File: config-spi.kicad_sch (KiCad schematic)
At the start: 40 parts, among them J1 878321412, Q7 BSS138APW, Q8 BSS138APW, U15 XC7K160T-FFG676, U3 S25FL128SAGNFI000

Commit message: Update PCB naming
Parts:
- C12: footprint data-center-dram-tester-footprints:0603-cap -> data-center-rdimm-ddr4-tester-footprints:0603-cap; symbol data-center-dram-tester:C_47u_0603 -> data-center-rdimm-ddr4-tester:C_47u_0603
- C13, C37: footprint data-center-dram-tester-footprints:0402-cap -> data-center-rdimm-ddr4-tester-footprints:0402-cap; symbol data-center-dram-tester:C_470n_0402 -> data-center-rdimm-ddr4-tester:C_470n_0402
- C5: footprint data-center-dram-tester-footprints:0402-cap -> data-center-rdimm-ddr4-tester-footprints:0402-cap; symbol data-center-dram-tester:C_100n_0402 -> data-center-rdimm-ddr4-tester:C_100n_0402
- D1, D10: footprint data-center-dram-tester-footprints:LED_0603 -> data-center-rdimm-ddr4-tester-footprints:LED_0603; symbol data-center-dram-tester:KP-1608CGCK -> data-center-rdimm-ddr4-tester:KP-1608CGCK
- D4: footprint data-center-dram-tester-footprints:TPD6E05U06 -> data-center-rdimm-ddr4-tester-footprints:TPD6E05U06; symbol data-center-dram-tester:TPD6E05U06 -> data-center-rdimm-ddr4-tester:TPD6E05U06
- EMCCLK1, PUDC_B1: footprint data-center-dram-tester-footprints:Testpoint_smd_1mm -> data-center-rdimm-ddr4-tester-footprints:Testpoint_smd_1mm; symbol data-center-dram-tester:TP_SMD1MM -> data-center-rdimm-ddr4-tester:TP_SMD1MM
- J1: footprint data-center-dram-tester-footprints:PinHeader_2x7_P2mm_SMD_no_locator -> data-center-rdimm-ddr4-tester-footprints:PinHeader_2x7_P2mm_SMD_no_locator; symbol data-center-dram-tester:878321412 -> data-center-rdimm-ddr4-tester:878321412
- PROG_B1: footprint data-center-dram-tester-footprints:Switch_Tactile_SMD_B3U-1000P -> data-center-rdimm-ddr4-tester-footprints:Switch_Tactile_SMD_B3U-1000P; symbol data-center-dram-tester:B3U-1000P -> data-center-rdimm-ddr4-tester:B3U-1000P
- Q7, Q8: footprint data-center-dram-tester-footprints:SC70-3 -> data-center-rdimm-ddr4-tester-footprints:SC70-3; symbol data-center-dram-tester:BSS138APW -> data-center-rdimm-ddr4-tester:BSS138APW
- R10, R33, R34, R36: footprint data-center-dram-tester-footprints:0402-res -> data-center-rdimm-ddr4-tester-footprints:0402-res; symbol data-center-dram-tester:R_100R_0402 -> data-center-rdimm-ddr4-tester:R_100R_0402
- R11, R12, R13, R23, R24, R26, R27, R58, R59, R60, R9: footprint data-center-dram-tester-footprints:0402-res -> data-center-rdimm-ddr4-tester-footprints:0402-res; symbol data-center-dram-tester:R_0R_0402 -> data-center-rdimm-ddr4-tester:R_0R_0402
- R14: footprint data-center-dram-tester-footprints:0402-res -> data-center-rdimm-ddr4-tester-footprints:0402-res; symbol data-center-dram-tester:R_2k2_0402 -> data-center-rdimm-ddr4-tester:R_2k2_0402
- R193: footprint data-center-dram-tester-footprints:0402-res -> data-center-rdimm-ddr4-tester-footprints:0402-res; symbol data-center-dram-tester:R_10k_0402 -> data-center-rdimm-ddr4-tester:R_10k_0402
- R21, R22, R28, R32: footprint data-center-dram-tester-footprints:0402-res -> data-center-rdimm-ddr4-tester-footprints:0402-res; symbol data-center-dram-tester:R_4k7_0402 -> data-center-rdimm-ddr4-tester:R_4k7_0402
- R30, R31, R57: footprint data-center-dram-tester-footprints:0402-res -> data-center-rdimm-ddr4-tester-footprints:0402-res; symbol data-center-dram-tester:R_330R_0402 -> data-center-rdimm-ddr4-tester:R_330R_0402
- S2: footprint data-center-dram-tester-footprints:SW_DS04-254-1-01BK-SMT -> data-center-rdimm-ddr4-tester-footprints:SW_DS04-254-1-01BK-SMT; symbol data-center-dram-tester:DS04-254-1-01BK-SMT -> data-center-rdimm-ddr4-tester:DS04-254-1-01BK-SMT
- U15: footprint data-center-dram-tester-footprints:xc7k160tfbg676 -> data-center-rdimm-ddr4-tester-footprints:xc7k160tfbg676; symbol data-center-dram-tester:XC7K160T-FFG676 -> data-center-rdimm-ddr4-tester:XC7K160T-FFG676
- U3: footprint data-center-dram-tester-footprints:WSON8x6_WSON6x5_dual -> data-center-rdimm-ddr4-tester-footprints:WSON8x6_WSON6x5_dual; symbol data-center-dram-tester:S25FL128SAGNFI000 -> data-center-rdimm-ddr4-tester:S25FL128SAGNFI000
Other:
- title: Data Center DRAM Tester -> Data Center RDIMM DDR4 Tester

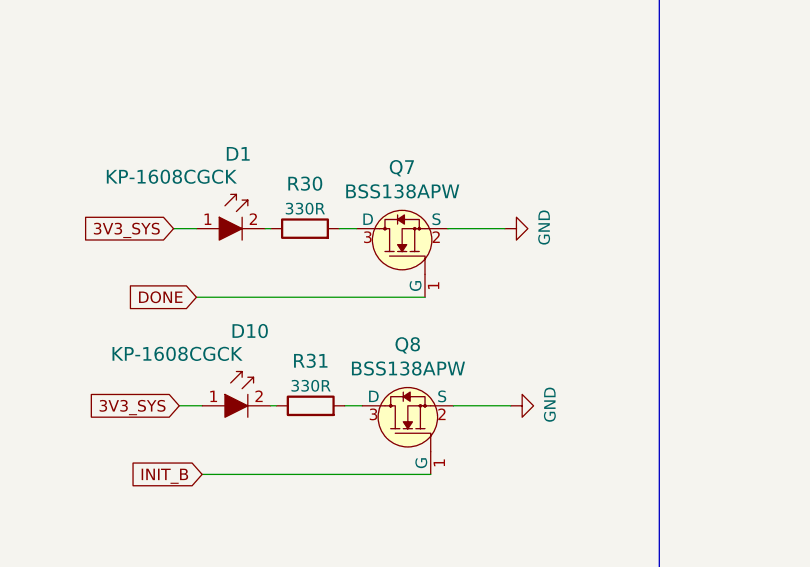
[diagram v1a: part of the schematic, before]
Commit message: Update BSS138PW lib name and MPN
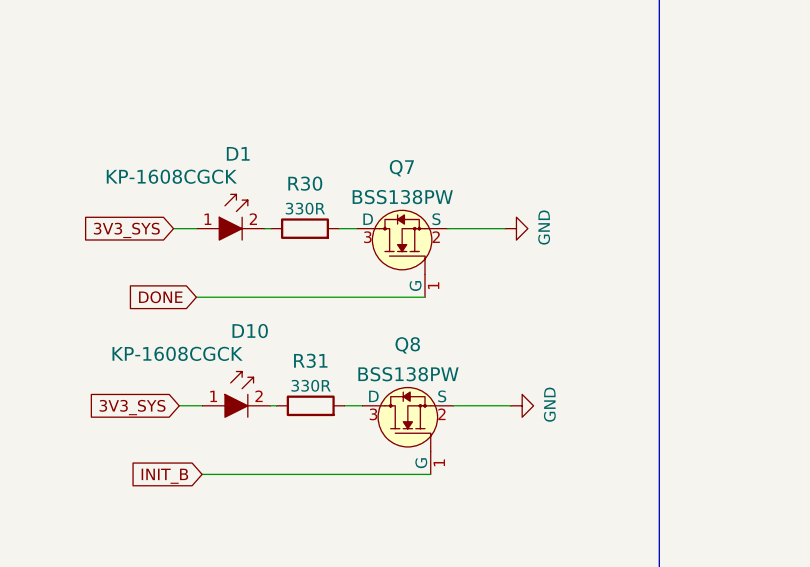
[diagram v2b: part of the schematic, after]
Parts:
- Q7, Q8: value BSS138APW -> BSS138PW; footprint data-center-rdimm-ddr4-tester-footprints:SC70-3 -> antmicro-footprints:SC70-3; symbol data-center-rdimm-ddr4-tester:BSS138APW -> data-center-rdimm-ddr4-tester:BSS138PW; Manufacturer ON Semiconductor -> Nexperia
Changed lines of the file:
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@@
     (pin "2")
   )
-  (symbol (lib_id "data-center-rdimm-ddr4-tester:BSS138APW") (at 167.005 238.125 90) (unit 1)
+  (symbol (lib_id "data-center-rdimm-ddr4-tester:BSS138PW") (at 167.005 238.125 90) (unit 1)
     (in_bom yes) (on_board yes)
     (property "Reference" "Q7" (id 0) (at 167.005 231.3432 90)
       (effects (font (size 1.524 1.524)))
     )
-    (property "Value" "BSS138APW" (id 1) (at 167.005 234.0356 90)
+    (property "Value" "BSS138PW" (id 1) (at 167.005 234.6706 90)
       (effects (font (size 1.524 1.524)))
     )
-    (property "Footprint" "data-center-rdimm-ddr4-tester-footprints:SC70-3" (id 2) (at 161.925 233.045 0)
+    (property "Footprint" "antmicro-footprints:SC70-3" (id 2) (at 161.925 233.045 0)
       (effects (font (size 1.524 1.524)) (justify left) hide)
     )
-    (property "Datasheet" "" (id 3) (at 159.385 233.045 0)
+    (property "Datasheet" "https://assets.nexperia.com/documents/data-sheet/BSS138PW.pdf" (id 3) (at 159.385 233.045 0)
       (effects (font (size 1.524 1.524)) (justify left) hide)
     )
-    (property "MPN" "BSS138PW" (id 4) (at 154.305 233.045 0)
+    (property "MPN" "BSS138PW" (id 4) (at 156.845 221.615 0)
       (effects (font (size 1.524 1.524)) (justify left) hide)
     )
-    (property "Manufacturer" "ON Semiconductor" (id 5) (at 139.065 233.045 0)
+    (property "Manufacturer" "Nexperia" (id 5) (at 156.845 233.045 0)
       (effects (font (size 1.524 1.524)) (justify left) hide)
     )
@@
     (pin "3")
   )
-  (symbol (lib_id "data-center-rdimm-ddr4-tester:BSS138APW") (at 167.64 257.81 90) (unit 1)
+  (symbol (lib_id "data-center-rdimm-ddr4-tester:BSS138PW") (at 167.64 257.81 90) (unit 1)
     (in_bom yes) (on_board yes)
     (property "Reference" "Q8" (id 0) (at 167.64 251.0282 90)
       (effects (font (size 1.524 1.524)))
     )
-    (property "Value" "BSS138APW" (id 1) (at 167.64 253.7206 90)
+    (property "Value" "BSS138PW" (id 1) (at 167.64 254.3556 90)
       (effects (font (size 1.524 1.524)))
     )
-    (property "Footprint" "data-center-rdimm-ddr4-tester-footprints:SC70-3" (id 2) (at 162.56 252.73 0)
+    (property "Footprint" "antmicro-footprints:SC70-3" (id 2) (at 162.56 252.73 0)
       (effects (font (size 1.524 1.524)) (justify left) hide)
     )
-    (property "Datasheet" "" (id 3) (at 160.02 252.73 0)
+    (property "Datasheet" "https://assets.nexperia.com/documents/data-sheet/BSS138PW.pdf" (id 3) (at 160.02 252.73 0)
       (effects (font (size 1.524 1.524)) (justify left) hide)
     )
-    (property "MPN" "BSS138PW" (id 4) (at 154.94 252.73 0)
+    (property "MPN" "BSS138PW" (id 4) (at 157.48 241.3 0)
       (effects (font (size 1.524 1.524)) (justify left) hide)
     )
-    (property "Manufacturer" "ON Semiconductor" (id 5) (at 139.7 252.73 0)
+    (property "Manufacturer" "Nexperia" (id 5) (at 157.48 252.73 0)
       (effects (font (size 1.524 1.524)) (justify left) hide)
     )

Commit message: Introduce component standardization
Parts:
- C12: footprint data-center-rdimm-ddr4-tester-footprints:0603-cap -> data-center-rdimm-ddr4-tester-footprints:C_0603_1608Metric; Author (none) -> Antmicro; License (none) -> Apache-2.0; Manufacturer MURATA -> Murata
- C13, C37: footprint data-center-rdimm-ddr4-tester-footprints:0402-cap -> data-center-rdimm-ddr4-tester-footprints:C_0402_1005Metric; Author (none) -> Antmicro; License (none) -> Apache-2.0
- C5: footprint data-center-rdimm-ddr4-tester-footprints:0402-cap -> data-center-rdimm-ddr4-tester-footprints:C_0402_1005Metric; Author (none) -> Antmicro; Dielectric (none) -> X5R; License (none) -> Apache-2.0; Voltage (none) -> 50V
- D1, D10: value KP-1608CGCK -> LED_G_0603_KP-1608CGCK; footprint data-center-rdimm-ddr4-tester-footprints:LED_0603 -> data-center-rdimm-ddr4-tester-footprints:LED_0603_1608Metric_G; symbol data-center-rdimm-ddr4-tester:KP-1608CGCK -> data-center-rdimm-ddr4-tester:LED_G_0603_KP-1608CGCK; Author (none) -> Antmicro; License (none) -> Apache-2.0; Manufacturer KINGBRIGHT -> Kingbright
- D4: value TPD6E05U06 -> TPD6E05U06RVZR; footprint data-center-rdimm-ddr4-tester-footprints:TPD6E05U06 -> data-center-rdimm-ddr4-tester-footprints:USON-14_3.5X1.3X0.5mm_P0.5mm; symbol data-center-rdimm-ddr4-tester:TPD6E05U06 -> data-center-rdimm-ddr4-tester:TPD6E05U06RVZR; Author (none) -> Antmicro; License (none) -> Apache-2.0
- EMCCLK1, PUDC_B1: value TP_SMD1MM -> TP_1mm_SMD; symbol data-center-rdimm-ddr4-tester:TP_SMD1MM -> data-center-rdimm-ddr4-tester:TP_1mm_SMD; Author (none) -> Antmicro; License (none) -> Apache-2.0
- J1: value 878321412 -> PinHeader_2x7_P2mm_SMD_Shrouded_no-locator; footprint data-center-rdimm-ddr4-tester-footprints:PinHeader_2x7_P2mm_SMD_no_locator -> data-center-rdimm-ddr4-tester-footprints:PinHeader_2x7_P2mm_SMD_Shrouded_no-locator; symbol data-center-rdimm-ddr4-tester:878321412 -> data-center-rdimm-ddr4-tester:PinHeader_2x7_P2mm_SMD_Shrouded_no-locator; Author (none) -> Antmicro; License (none) -> Apache-2.0
- PROG_B1: value B3U-1000P -> SW_B3U-1000P; footprint data-center-rdimm-ddr4-tester-footprints:Switch_Tactile_SMD_B3U-1000P -> data-center-rdimm-ddr4-tester-footprints:SW_B3U-3000P; symbol data-center-rdimm-ddr4-tester:B3U-1000P -> data-center-rdimm-ddr4-tester:SW_B3U-1000P; Author (none) -> Antmicro; License (none) -> Apache-2.0; Manufacturer Omron Electronics Inc-EMC Div -> Omron Electronics
- Q7, Q8: footprint antmicro-footprints:SC70-3 -> data-center-rdimm-ddr4-tester-footprints:SC70-3; Author (none) -> Antmicro; License (none) -> Apache-2.0
- R10, R33, R34, R36: footprint data-center-rdimm-ddr4-tester-footprints:0402-res -> data-center-rdimm-ddr4-tester-footprints:R_0402_1005Metric; Author (none) -> Antmicro; License (none) -> Apache-2.0; Manufacturer BOURNS -> Bourns; Tolerance (none) -> 1%
- R11, R12, R13, R23, R24, R26, R27, R58, R59, R60, R9: footprint data-center-rdimm-ddr4-tester-footprints:0402-res -> data-center-rdimm-ddr4-tester-footprints:R_0402_1005Metric; Author (none) -> Antmicro; Current (none) -> 1A; License (none) -> Apache-2.0; Manufacturer PANASONIC -> Panasonic
- R14: footprint data-center-rdimm-ddr4-tester-footprints:0402-res -> data-center-rdimm-ddr4-tester-footprints:R_0402_1005Metric; Author (none) -> Antmicro; License (none) -> Apache-2.0; MPN RC0402FR-072K2L -> CR0402-FX-2201GLF; Manufacturer YAGEO -> Bourns; Tolerance (none) -> 1%
- R193: footprint data-center-rdimm-ddr4-tester-footprints:0402-res -> data-center-rdimm-ddr4-tester-footprints:R_0402_1005Metric; Author (none) -> Antmicro; License (none) -> Apache-2.0; MPN CRCW040210K0FKEDHP -> CR0402-FX-1002GLF; Manufacturer VISHAY -> Bourns; Tolerance (none) -> 1%
- R21, R22, R28, R32: footprint data-center-rdimm-ddr4-tester-footprints:0402-res -> data-center-rdimm-ddr4-tester-footprints:R_0402_1005Metric; Author (none) -> Antmicro; License (none) -> Apache-2.0; MPN ERJ2GEJ472X -> CR0402-FX-4701GLF; Manufacturer PANASONIC_ELECTRONIC_COMPONENTS -> Bourns; Tolerance (none) -> 1%
- R30, R31, R57: footprint data-center-rdimm-ddr4-tester-footprints:0402-res -> data-center-rdimm-ddr4-tester-footprints:R_0402_1005Metric; Author (none) -> Antmicro; License (none) -> Apache-2.0; MPN MCMR04X3300FTL -> CR0402-FX-3300GLF; Manufacturer MULTICOMP -> Bourns; Tolerance (none) -> 1%
- S2: value DS04-254-1-01BK-SMT -> SW_DS04-254-1-01BK-SMT; symbol data-center-rdimm-ddr4-tester:DS04-254-1-01BK-SMT -> data-center-rdimm-ddr4-tester:SW_DS04-254-1-01BK-SMT; Author (none) -> Antmicro; License (none) -> Apache-2.0; Manufacturer CUI Devices -> CUI Inc
- U15: footprint data-center-rdimm-ddr4-tester-footprints:xc7k160tfbg676 -> data-center-rdimm-ddr4-tester-footprints:BGA-676_27x27mm_Layout26x26_P1X1mm; Author (none) -> Antmicro; License (none) -> Apache-2.0; MPN (none) -> XC7K160T-FFG676; Manufacturer (none) -> Xilinx
- U3: footprint data-center-rdimm-ddr4-tester-footprints:WSON8x6_WSON6x5_dual -> data-center-rdimm-ddr4-tester-footprints:WSON-8_6x8x0.5mm_P1.27mm; Author (none) -> Antmicro; License (none) -> Apache-2.0
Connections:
- net 3V3_SYS: now also R14.1; no longer R14.2
- net FCS_B: now also R14.2; no longer R14.1
- net TCK_JTAG: now also D4.2 (D1-)
- net TDI_JTAG: now also D4.7 (D3-)
- net TDO_JTAG: now also D4.6 (D3+)
- net TMS_JTAG: now also D4.1 (D1+)
- net at D4.11 (D2-): now also D4.4 (D2-)
- net at D4.12 (D2+): now also D4.3 (D2+)
- no-connect marks 2 -> 4
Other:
- note added: "000 001 010 100 101 110 111"
- note added: "Config. mode"
- note added: "MODE[2:0]"
- note added: "Master Serial Master SPI Master BPI Master SelectMAP JTAG Slave SelectMAP Slave Serial"
- note removed: "Config. mode Master Serial Master SPI Master BPI Master SelectMAP JTAG Slave SelectMAP Slave Serial"
- note removed: "MODE[2:0] 000 001 010 100 101 110 111"
- moved on the sheet: C12, C13, C37, C5, EMCCLK1, PUDC_B1, R10, R14, R193, R21, R22, R23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

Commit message: [#55119] component update
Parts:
- C12: footprint data-center-rdimm-ddr4-tester-footprints:C_0603_1608Metric -> antmicro-footprints:C_0603_1608Metric; symbol data-center-rdimm-ddr4-tester:C_47u_0603 -> antmicroCapacitors0603:C_47u_0603
- C13, C37: footprint data-center-rdimm-ddr4-tester-footprints:C_0402_1005Metric -> antmicro-footprints:C_0402_1005Metric; symbol data-center-rdimm-ddr4-tester:C_470n_0402 -> antmicroCapacitors0402:C_470n_0402
- C5: footprint data-center-rdimm-ddr4-tester-footprints:C_0402_1005Metric -> antmicro-footprints:C_0402_1005Metric; symbol data-center-rdimm-ddr4-tester:C_100n_0402 -> antmicroCapacitors0402:C_100n_0402
- D1, D10: footprint data-center-rdimm-ddr4-tester-footprints:LED_0603_1608Metric_G -> antmicro-footprints:LED_0603_1608Metric_G; symbol data-center-rdimm-ddr4-tester:LED_G_0603_KP-1608CGCK -> antmicroLEDIndicationDiscrete:LED_G_0603_KP-1608CGCK
- D4: footprint data-center-rdimm-ddr4-tester-footprints:USON-14_3.5X1.3X0.5mm_P0.5mm -> antmicro-footprints:USON-14_3.5X1.3X0.5mm_P0.5mm; symbol data-center-rdimm-ddr4-tester:TPD6E05U06RVZR -> antmicroTVSDiodes:TPD6E05U06RVZR; now not fitted; now left out of the parts list
- EMCCLK1, PUDC_B1: footprint data-center-rdimm-ddr4-tester-footprints:Testpoint_smd_1mm -> antmicro-footprints:TP_SMD_1mm; symbol data-center-rdimm-ddr4-tester:TP_1mm_SMD -> antmicroTestPoints:TP_1mm_SMD
- J1: footprint data-center-rdimm-ddr4-tester-footprints:PinHeader_2x7_P2mm_SMD_Shrouded_no-locator -> antmicro-footprints:PinHeader_2x7_P2mm_SMD_Shrouded_no-locator; symbol data-center-rdimm-ddr4-tester:PinHeader_2x7_P2mm_SMD_Shrouded_no-locator -> antmicroGenericPinHeaders:PinHeader_2x7_P2mm_SMD_Shrouded_no-locator; now not fitted; now left out of the parts list
- PROG_B1: footprint data-center-rdimm-ddr4-tester-footprints:SW_B3U-3000P -> antmicro-footprints:SW_B3U-1000P_SMD; symbol data-center-rdimm-ddr4-tester:SW_B3U-1000P -> antmicroPushbuttonSwitches:SW_B3U-1000P_SMD; Manufacturer Omron Electronics -> Omron
- Q7, Q8: footprint data-center-rdimm-ddr4-tester-footprints:SC70-3 -> antmicro-footprints:SC70-3; symbol data-center-rdimm-ddr4-tester:BSS138PW -> antmicroTransistorsFETsMOSFETsSingle:BSS138PW
- R10: footprint data-center-rdimm-ddr4-tester-footprints:R_0402_1005Metric -> antmicro-footprints:R_0402_1005Metric; symbol data-center-rdimm-ddr4-tester:R_100R_0402 -> antmicroResistors0402:R_100R_0402
- R11, R12: footprint data-center-rdimm-ddr4-tester-footprints:R_0402_1005Metric -> antmicro-footprints:R_0402_1005Metric; symbol data-center-rdimm-ddr4-tester:R_0R_0402 -> antmicroResistors0402:R_0R_0402; now not fitted; now left out of the parts list
- R13, R23, R24, R26, R27, R58, R59, R60, R9: footprint data-center-rdimm-ddr4-tester-footprints:R_0402_1005Metric -> antmicro-footprints:R_0402_1005Metric; symbol data-center-rdimm-ddr4-tester:R_0R_0402 -> antmicroResistors0402:R_0R_0402
- R14: footprint data-center-rdimm-ddr4-tester-footprints:R_0402_1005Metric -> antmicro-footprints:R_0402_1005Metric; symbol data-center-rdimm-ddr4-tester:R_2k2_0402 -> antmicroResistors0402:R_2k2_0402
- R193: footprint data-center-rdimm-ddr4-tester-footprints:R_0402_1005Metric -> antmicro-footprints:R_0402_1005Metric; symbol data-center-rdimm-ddr4-tester:R_10k_0402 -> antmicroResistors0402:R_10k_0402
- R21, R22, R28, R32: footprint data-center-rdimm-ddr4-tester-footprints:R_0402_1005Metric -> antmicro-footprints:R_0402_1005Metric; symbol data-center-rdimm-ddr4-tester:R_4k7_0402 -> antmicroResistors0402:R_4k7_0402
- R30, R31, R57: footprint data-center-rdimm-ddr4-tester-footprints:R_0402_1005Metric -> antmicro-footprints:R_0402_1005Metric; symbol data-center-rdimm-ddr4-tester:R_330R_0402 -> antmicroResistors0402:R_330R_0402
- R33, R34, R36: footprint data-center-rdimm-ddr4-tester-footprints:R_0402_1005Metric -> antmicro-footprints:R_0402_1005Metric; symbol data-center-rdimm-ddr4-tester:R_100R_0402 -> antmicroResistors0402:R_100R_0402; now not fitted; now left out of the parts list
- S2: footprint data-center-rdimm-ddr4-tester-footprints:SW_DS04-254-1-01BK-SMT -> antmicro-footprints:SW_DS04-254-1-01BK-SMT; symbol data-center-rdimm-ddr4-tester:SW_DS04-254-1-01BK-SMT -> antmicroSlideSwitches:SW_DS04-254-1-01BK-SMT
- U15: footprint data-center-rdimm-ddr4-tester-footprints:BGA-676_27x27mm_Layout26x26_P1X1mm -> antmicro-footprints:BGA-676_27x27mm_Layout26x26_P1X1mm; symbol data-center-rdimm-ddr4-tester:XC7K160T-FFG676 -> antmicroMicrocontrollers:XC7K160T-FFG676; Manufacturer Xilinx -> AMD-Xilinx
- U3: footprint data-center-rdimm-ddr4-tester-footprints:WSON-8_6x8x0.5mm_P1.27mm -> antmicro-footprints:WSON-8_6x8x0.5mm_P1.27mm; symbol data-center-rdimm-ddr4-tester:S25FL128SAGNFI000 -> antmicroMemory:S25FL128SAGNFI000
